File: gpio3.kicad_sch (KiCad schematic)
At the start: 3 parts, among them U27 RK3576

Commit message: Add files via upload
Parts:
- renumbered C327 to C100, C326 to C101, U27 to U2
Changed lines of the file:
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@@
 		(dnp no)
 		(fields_autoplaced yes)
-		(property "Reference" "C327"
+		(property "Reference" "C100"
 			(at 62.23 41.9162 0)
 			(show_name no)
@@
 		)
 		(property "Description" "Unpolarized capacitor, small symbol"
+			(at 59.69 43.18 0)
+			(hide yes)
+			(show_name no)
+			(do_not_autoplace no)
+			(effects
+				(font
+					(size 1.27 1.27)
+				)
+			)
+		)
+		(property "Dielectric" ""
+			(at 59.69 43.18 0)
+			(hide yes)
+			(show_name no)
+			(do_not_autoplace no)
+			(effects
+				(font
+					(size 1.27 1.27)
+				)
+			)
+		)
+		(property "Voltage" ""
+			(at 59.69 43.18 0)
+			(hide yes)
+			(show_name no)
+			(do_not_autoplace no)
+			(effects
+				(font
+					(size 1.27 1.27)
+				)
+			)
+		)
+		(property "KLC_S3.3" ""
+			(at 59.69 43.18 0)
+			(hide yes)
+			(show_name no)
+			(do_not_autoplace no)
+			(effects
+				(font
+					(size 1.27 1.27)
+				)
+			)
+		)
+		(property "KLC_S4.1" ""
+			(at 59.69 43.18 0)
+			(hide yes)
+			(show_name no)
+			(do_not_autoplace no)
+			(effects
+				(font
+					(size 1.27 1.27)
+				)
+			)
+		)
+		(property "KLC_S5.1" ""
 			(at 59.69 43.18 0)
 			(hide yes)
@@
 			(project "RK3576 SBC"
 				(path "/b79dbff4-0cad-4ff7-bec2-7c0e4f8b14d3/34f9b0cb-aeae-42b4-a2af-a0a79afcf392/5c5b5f2c-d981-472c-a803-168d99f2d260"
-					(reference "C327")
+					(reference "C100")
 					(unit 1)
 				)
@@
 		(in_pos_files yes)
 		(dnp no)
-		(property "Reference" "#PWR0421"
+		(property "Reference" "#PWR0138"
 			(at 59.69 44.45 0)
 			(hide yes)
@@
 			(project "RK3576 SBC"
 				(path "/b79dbff4-0cad-4ff7-bec2-7c0e4f8b14d3/34f9b0cb-aeae-42b4-a2af-a0a79afcf392/5c5b5f2c-d981-472c-a803-168d99f2d260"
-					(reference "#PWR0421")
+					(reference "#PWR0138")
 					(unit 1)
 				)
@@
 		(in_pos_files yes)
 		(dnp no)
-		(property "Reference" "#PWR0423"
+		(property "Reference" "#PWR0139"
 			(at 59.69 52.07 0)
 			(hide yes)
@@
 			(project "RK3576 SBC"
 				(path "/b79dbff4-0cad-4ff7-bec2-7c0e4f8b14d3/34f9b0cb-aeae-42b4-a2af-a0a79afcf392/5c5b5f2c-d981-472c-a803-168d99f2d260"
-					(reference "#PWR0423")
+					(reference "#PWR0139")
 					(unit 1)
 				)
@@
 		(in_pos_files yes)
 		(dnp no)
-		(property "Reference" "#PWR0422"
+		(property "Reference" "#PWR0140"
 			(at 69.85 52.07 0)
 			(hide yes)
@@
 			(project "RK3576 SBC"
 				(path "/b79dbff4-0cad-4ff7-bec2-7c0e4f8b14d3/34f9b0cb-aeae-42b4-a2af-a0a79afcf392/5c5b5f2c-d981-472c-a803-168d99f2d260"
-					(reference "#PWR0422")
+					(reference "#PWR0140")
 					(unit 1)
 				)
@@
 		(in_pos_files yes)
 		(dnp no)
-		(property "Reference" "U27"
-			(at 110.236 24.892 0)
+		(property "Reference" "U2"
+			(at 109.982 32.766 0)
 			(show_name no)
 			(do_not_autoplace no)
@@
 		)
 		(property "Value" "RK3576"
-			(at 110.236 27.432 0)
+			(at 109.982 35.306 0)
 			(show_name no)
 			(do_not_autoplace no)
@@
 		(property "Manf" "Rockchip"
 			(at 110.236 29.972 0)
+			(hide yes)
 			(show_name no)
 			(do_not_autoplace no)
@@
 		(property "MPN" "RK3576"
 			(at 110.236 32.512 0)
+			(hide yes)
 			(show_name no)
 			(do_not_autoplace no)
@@
 		(property "Package" "FCCSP698L"
 			(at 110.236 35.052 0)
+			(hide yes)
+			(show_name no)
+			(do_not_autoplace no)
+			(effects
+				(font
+					(size 1.27 1.27)
+				)
+			)
+		)
+		(property "Dielectric" ""
+			(at 110.49 64.77 0)
+			(hide yes)
+			(show_name no)
+			(do_not_autoplace no)
+			(effects
+				(font
+					(size 1.27 1.27)
+				)
+			)
+		)
+		(property "Voltage" ""
+			(at 110.49 64.77 0)
+			(hide yes)
+			(show_name no)
+			(do_not_autoplace no)
+			(effects
+				(font
+					(size 1.27 1.27)
+				)
+			)
+		)
+		(property "KLC_S3.3" ""
+			(at 110.49 64.77 0)
+			(hide yes)
+			(show_name no)
+			(do_not_autoplace no)
+			(effects
+				(font
+					(size 1.27 1.27)
+				)
+			)
+		)
+		(property "KLC_S4.1" ""
+			(at 110.49 64.77 0)
+			(hide yes)
+			(show_name no)
+			(do_not_autoplace no)
+			(effects
+				(font
+					(size 1.27 1.27)
+				)
+			)
+		)
+		(property "KLC_S5.1" ""
+			(at 110.49 64.77 0)
+			(hide yes)
 			(show_name no)
 			(do_not_autoplace no)
@@
 			(project "RK3576 SBC"
 				(path "/b79dbff4-0cad-4ff7-bec2-7c0e4f8b14d3/34f9b0cb-aeae-42b4-a2af-a0a79afcf392/5c5b5f2c-d981-472c-a803-168d99f2d260"
-					(reference "U27")
+					(reference "U2")
 					(unit 4)
 				)
@@
 		(dnp no)
 		(fields_autoplaced yes)
-		(property "Reference" "C326"
+		(property "Reference" "C101"
 			(at 72.39 41.9162 0)
 			(show_name no)
@@
 		)
 		(property "Description" "Unpolarized capacitor, small symbol"
+			(at 69.85 43.18 0)
+			(hide yes)
+			(show_name no)
+			(do_not_autoplace no)
+			(effects
+				(font
+					(size 1.27 1.27)
+				)
+			)
+		)
+		(property "Dielectric" ""
+			(at 69.85 43.18 0)
+			(hide yes)
+			(show_name no)
+			(do_not_autoplace no)
+			(effects
+				(font
+					(size 1.27 1.27)
+				)
+			)
+		)
+		(property "Voltage" ""
+			(at 69.85 43.18 0)
+			(hide yes)
+			(show_name no)
+			(do_not_autoplace no)
+			(effects
+				(font
+					(size 1.27 1.27)
+				)
+			)
+		)
+		(property "KLC_S3.3" ""
+			(at 69.85 43.18 0)
+			(hide yes)
+			(show_name no)
+			(do_not_autoplace no)
+			(effects
+				(font
+					(size 1.27 1.27)
+				)
+			)
+		)
+		(property "KLC_S4.1" ""
+			(at 69.85 43.18 0)
+			(hide yes)
+			(show_name no)
+			(do_not_autoplace no)
+			(effects
+				(font
+					(size 1.27 1.27)
+				)
+			)
+		)
+		(property "KLC_S5.1" ""
 			(at 69.85 43.18 0)
 			(hide yes)
@@
 			(project "RK3576 SBC"
 				(path "/b79dbff4-0cad-4ff7-bec2-7c0e4f8b14d3/34f9b0cb-aeae-42b4-a2af-a0a79afcf392/5c5b5f2c-d981-472c-a803-168d99f2d260"
-					(reference "C326")
+					(reference "C101")
 					(unit 1)
 				)

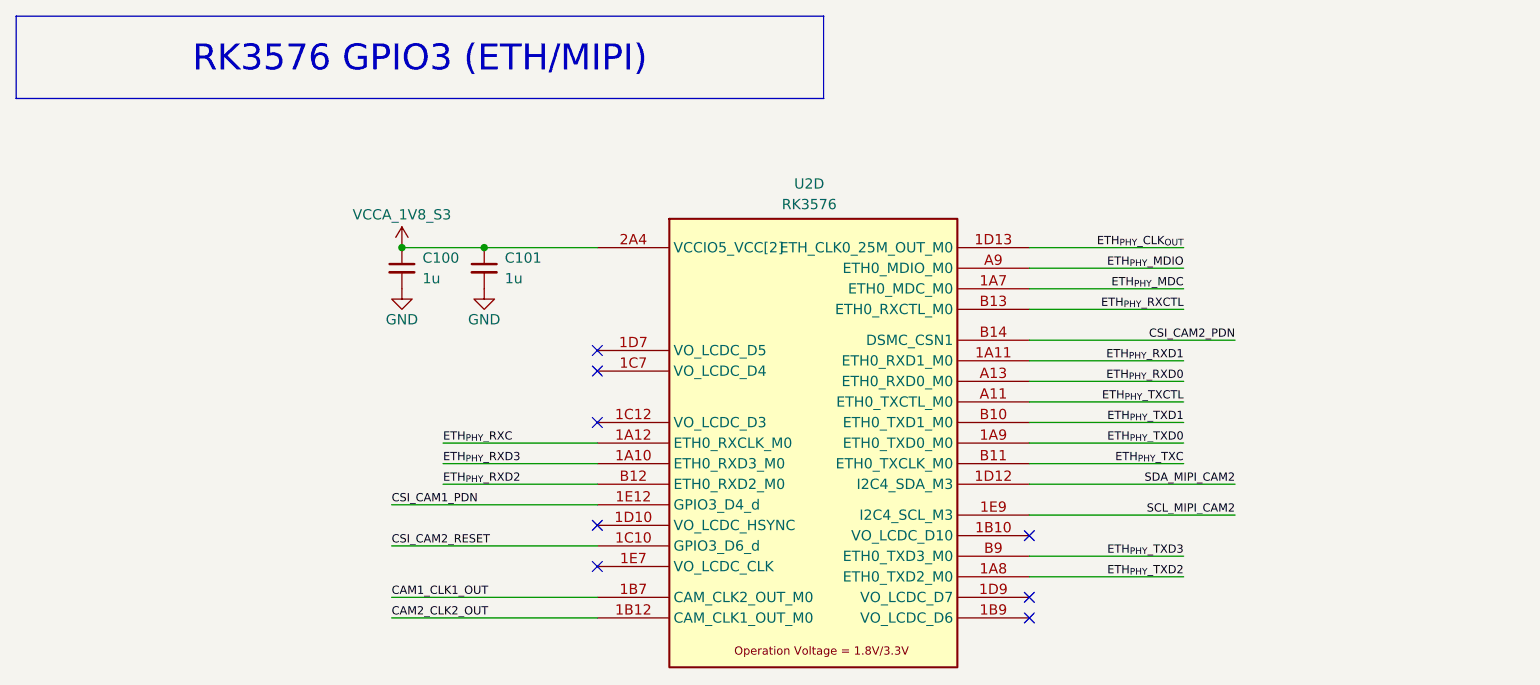
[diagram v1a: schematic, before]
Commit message: SBC Board V0.2
The SBC schematics before footprint and part number check
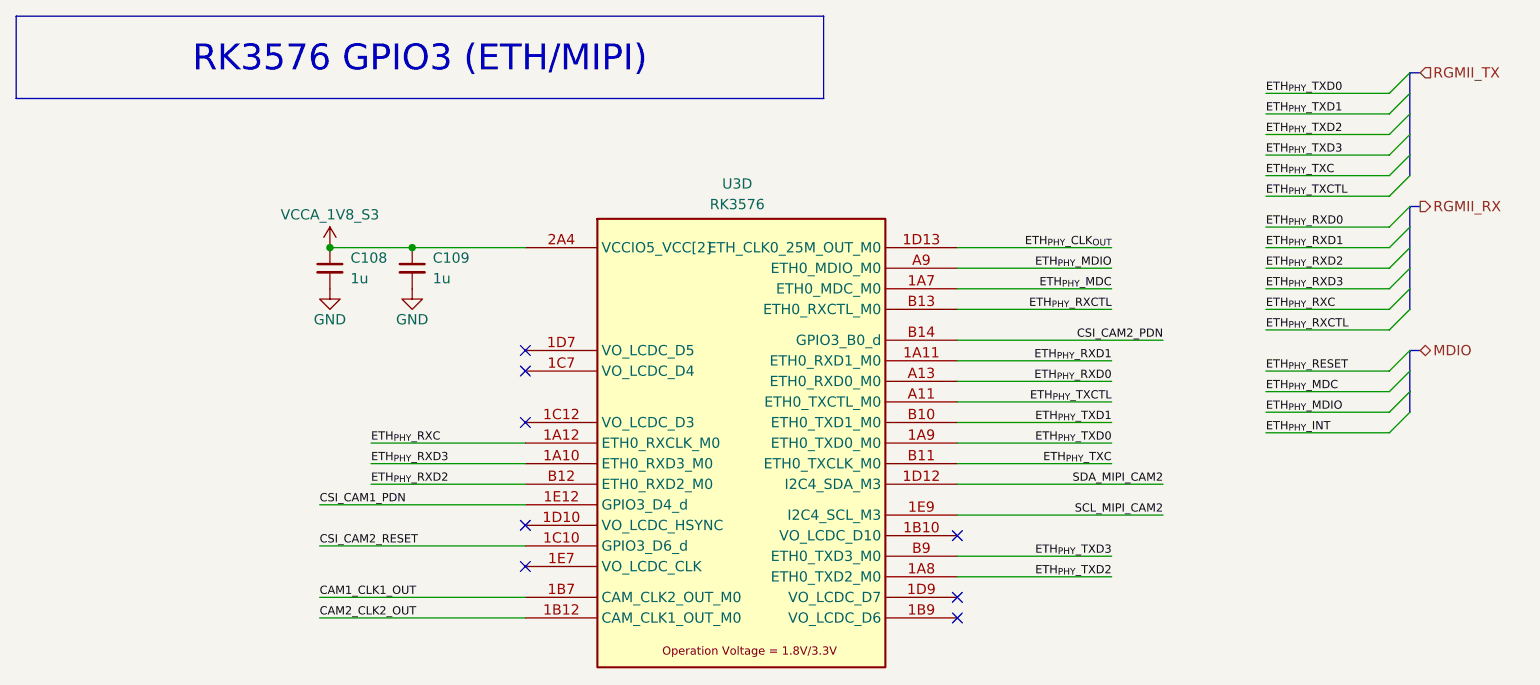
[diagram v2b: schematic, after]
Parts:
- U3: renamed from U2; footprint (none) -> easyeda2kicad:FCCSP-698_L17.2-W16.1-TL_RK3576
- renumbered C100 to C108, C101 to C109
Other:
- moved on the sheet: C108, C109, U3D

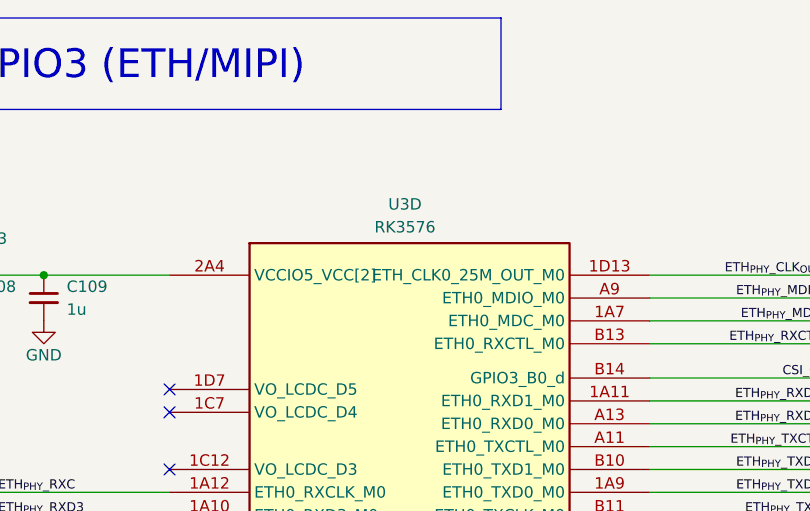
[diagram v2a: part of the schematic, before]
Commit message: SBCv0.3
there is no big thing update just some LCSC & Mouser parts
and Big problem deleted alot of component values (:
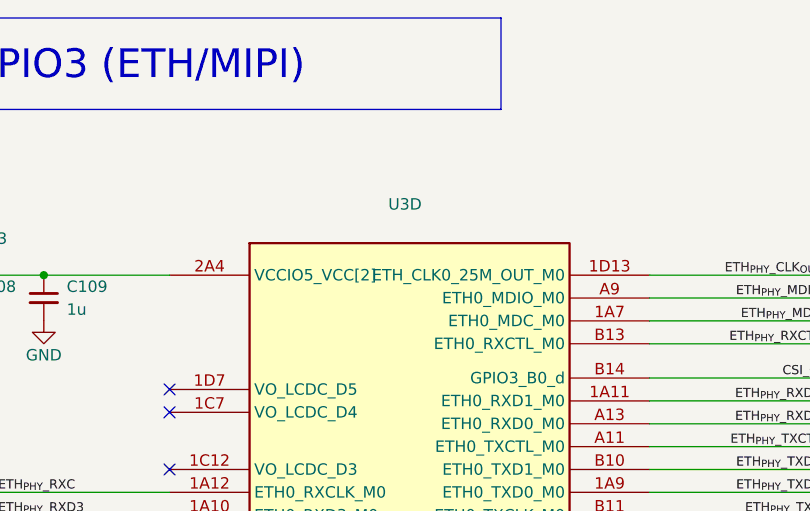
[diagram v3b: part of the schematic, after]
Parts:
- C108, C109: footprint Capacitor_SMD:C_0402_1005Metric_Pad0.74x0.62mm_HandSolder -> Capacitor_SMD:C_0201_0603Metric_Pad0.64x0.40mm_HandSolder; LCSC Part (none) -> C5209398; Mouser Part (none) -> CL03A105KP3NSNC
- U3: value RK3576 -> (none); LCSC Part (none) -> (polyline
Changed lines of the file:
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@@
 			)
 		)
-		(property "Footprint" "Capacitor_SMD:C_0402_1005Metric_Pad0.74x0.62mm_HandSolder"
+		(property "Footprint" "Capacitor_SMD:C_0201_0603Metric_Pad0.64x0.40mm_HandSolder"
 			(at 50.8 43.18 0)
 			(hide yes)
@@
 			)
 		)
-		(property "KLC_S5.1" ""
+		(property "LCSC Part" "C5209398"
+			(at 50.8 43.18 0)
+			(hide yes)
+			(show_name no)
+			(do_not_autoplace no)
+			(effects
+				(font
+					(size 1.27 1.27)
+				)
+			)
+		)
+		(property "Mouser Part" "CL03A105KP3NSNC "
+			(at 50.8 43.18 0)
+			(hide yes)
+			(show_name no)
+			(do_not_autoplace no)
+			(effects
+				(font
+					(size 1.27 1.27)
+				)
+			)
+		)
+		(property "KLC_S4.2_DVDD" ""
+			(at 50.8 43.18 0)
+			(hide yes)
+			(show_name no)
+			(do_not_autoplace no)
+			(effects
+				(font
+					(size 1.27 1.27)
+				)
+			)
+		)
+		(property "KLC_S4.2_VREG_LX" ""
 			(at 50.8 43.18 0)
 			(hide yes)
@@
 					(reference "C108")
 					(unit 1)
+					(variant
+						(name "Test")
+					)
 				)
 			)
@@
 			)
 		)
-		(property "Value" "RK3576"
+		(property "Value" ""
 			(at 101.092 35.306 0)
 			(show_name no)
@@
 			)
 		)
-		(property "KLC_S5.1" ""
+		(property "LCSC Part" "(polyline"
+			(at 101.6 64.77 0)
+			(hide yes)
+			(show_name no)
+			(do_not_autoplace no)
+			(effects
+				(font
+					(size 1.27 1.27)
+				)
+			)
+		)
+		(property "KLC_S4.2_DVDD" ""
+			(at 101.6 64.77 0)
+			(hide yes)
+			(show_name no)
+			(do_not_autoplace no)
+			(effects
+				(font
+					(size 1.27 1.27)
+				)
+			)
+		)
+		(property "KLC_S4.2_VREG_LX" ""
 			(at 101.6 64.77 0)
 			(hide yes)
@@
 					(reference "U3")
 					(unit 4)
+					(variant
+						(name "Test")
+					)
 				)
 			)
@@
 			)
 		)
-		(property "Footprint" "Capacitor_SMD:C_0402_1005Metric_Pad0.74x0.62mm_HandSolder"
+		(property "Footprint" "Capacitor_SMD:C_0201_0603Metric_Pad0.64x0.40mm_HandSolder"
 			(at 60.96 43.18 0)
 			(hide yes)
@@
 			)
 		)
-		(property "KLC_S5.1" ""
+		(property "LCSC Part" "C5209398"
+			(at 60.96 43.18 0)
+			(hide yes)
+			(show_name no)
+			(do_not_autoplace no)
+			(effects
+				(font
+					(size 1.27 1.27)
+				)
+			)
+		)
+		(property "Mouser Part" "CL03A105KP3NSNC "
+			(at 60.96 43.18 0)
+			(hide yes)
+			(show_name no)
+			(do_not_autoplace no)
+			(effects
+				(font
+					(size 1.27 1.27)
+				)
+			)
+		)
+		(property "KLC_S4.2_DVDD" ""
+			(at 60.96 43.18 0)
+			(hide yes)
+			(show_name no)
+			(do_not_autoplace no)
+			(effects
+				(font
+					(size 1.27 1.27)
+				)
+			)
+		)
+		(property "KLC_S4.2_VREG_LX" ""
 			(at 60.96 43.18 0)
 			(hide yes)
@@
 					(reference "C109")
 					(unit 1)
-				)
-			)
+					(variant
+						(name "Test")
+					)
+				)
+			)

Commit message: SBCv0.4
add LCSC & Mouser parts 
and solve the deleted value in the past version
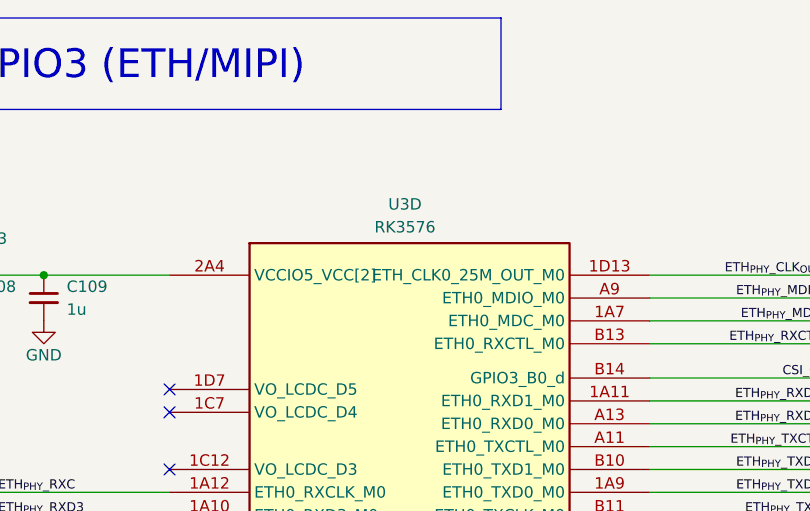
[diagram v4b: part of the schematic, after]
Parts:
- U3: value (none) -> RK3576; LCSC Part (polyline -> C42388007
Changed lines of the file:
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@@
 			)
 		)
-		(property "Value" ""
+		(property "Value" "RK3576"
 			(at 101.092 35.306 0)
 			(show_name no)
@@
 			)
 		)
-		(property "LCSC Part" "(polyline"
+		(property "LCSC Part" "C42388007"
 			(at 101.6 64.77 0)
 			(hide yes)
